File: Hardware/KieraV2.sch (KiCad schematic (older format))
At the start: 36 parts, among them J1 Conn_01x05_Male, J2 Conn_01x04_Male, SW1 SW_Rotary2x4, SW2 SW_Rotary2x4, SW3 SW_Push, SW4 SW_Push, SW5 SW_Push, SW6 SW_MEC_5G, U1 STM32L4P5RET6, Y1 8MHz

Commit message: removed resistor in crystal section
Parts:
- removed R16: 400, symbol Device:R
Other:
- moved on the sheet: C14, C15, C17, Y1
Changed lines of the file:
@@
 Text GLabel 5350 3600 0    50   Input ~ 0
 OSC_OUT
-Text GLabel 9350 2350 0    50   Input ~ 0
+Text GLabel 9450 2350 0    50   Input ~ 0
 OSC_OUT
 $Comp
 L Device:Crystal Y1
 U 1 1 61C845B0
-P 10050 2100
-F 0 "Y1" V 10004 2231 50  0000 L CNN
-F 1 "8MHz" V 10095 2231 50  0000 L CNN
-F 2 "" H 10050 2100 50  0001 C CNN
-F 3 "~" H 10050 2100 50  0001 C CNN
-	1    10050 2100
+P 9800 2100
+F 0 "Y1" V 9754 2231 50  0000 L CNN
+F 1 "8MHz" V 9845 2231 50  0000 L CNN
+F 2 "" H 9800 2100 50  0001 C CNN
+F 3 "~" H 9800 2100 50  0001 C CNN
+	1    9800 2100
 	0    1    1    0
 $EndComp
@@
 L Device:C C14
 U 1 1 61C8E389
-P 10500 1850
-F 0 "C14" V 10650 1800 50  0000 L CNN
-F 1 "10pF" V 10350 1750 50  0000 L CNN
-F 2 "" H 10538 1700 50  0001 C CNN
-F 3 "~" H 10500 1850 50  0001 C CNN
-	1    10500 1850
+P 10250 1850
+F 0 "C14" V 10400 1800 50  0000 L CNN
+F 1 "10pF" V 10100 1750 50  0000 L CNN
+F 2 "" H 10288 1700 50  0001 C CNN
+F 3 "~" H 10250 1850 50  0001 C CNN
+	1    10250 1850
 	0    -1   -1   0
 $EndComp
@@
 L Device:C C15
 U 1 1 61C92020
-P 10500 2350
-F 0 "C15" V 10650 2300 50  0000 L CNN
-F 1 "10pF" V 10350 2250 50  0000 L CNN
-F 2 "" H 10538 2200 50  0001 C CNN
-F 3 "~" H 10500 2350 50  0001 C CNN
-	1    10500 2350
+P 10250 2350
+F 0 "C15" V 10400 2300 50  0000 L CNN
+F 1 "10pF" V 10100 2250 50  0000 L CNN
+F 2 "" H 10288 2200 50  0001 C CNN
+F 3 "~" H 10250 2350 50  0001 C CNN
+	1    10250 2350
 	0    -1   -1   0
 $EndComp
@@
 L power:GND #PWR?
 U 1 1 61CA102A
-P 10850 2350
-F 0 "#PWR?" H 10850 2100 50  0001 C CNN
-F 1 "GND" H 10855 2177 50  0000 C CNN
-F 2 "" H 10850 2350 50  0001 C CNN
-F 3 "" H 10850 2350 50  0001 C CNN
-	1    10850 2350
-	1    0    0    -1
-$EndComp
-Wire Wire Line
-	10650 2350 10850 2350
-Wire Wire Line
-	10650 1850 10850 1850
-Wire Wire Line
-	10850 1850 10850 2350
-Connection ~ 10850 2350
-Wire Wire Line
-	10350 1850 10050 1850
-Wire Wire Line
-	10050 1950 10050 1850
-Wire Wire Line
-	10050 2250 10050 2350
-Text GLabel 9350 1850 0    50   Input ~ 0
+P 10600 2350
+F 0 "#PWR?" H 10600 2100 50  0001 C CNN
+F 1 "GND" H 10605 2177 50  0000 C CNN
+F 2 "" H 10600 2350 50  0001 C CNN
+F 3 "" H 10600 2350 50  0001 C CNN
+	1    10600 2350
+	1    0    0    -1
+$EndComp
+Wire Wire Line
+	10400 2350 10600 2350
+Wire Wire Line
+	10400 1850 10600 1850
+Wire Wire Line
+	10600 1850 10600 2350
+Connection ~ 10600 2350
+Wire Wire Line
+	10100 1850 9800 1850
+Wire Wire Line
+	9800 1950 9800 1850
+Wire Wire Line
+	9800 2250 9800 2350
+Text GLabel 9450 1850 0    50   Input ~ 0
 OSC_IN
-Connection ~ 10050 1850
-Wire Wire Line
-	10050 2350 10350 2350
-Wire Wire Line
-	9350 1850 10050 1850
-$Comp
-L Device:R R16
-U 1 1 61CD4DE5
-P 9700 2350
-F 0 "R16" V 9493 2350 50  0000 C CNN
-F 1 "400" V 9584 2350 50  0000 C CNN
-F 2 "" V 9630 2350 50  0001 C CNN
-F 3 "~" H 9700 2350 50  0001 C CNN
-	1    9700 2350
-	0    1    1    0
-$EndComp
-Wire Wire Line
-	9550 2350 9350 2350
-Wire Wire Line
-	9850 2350 10050 2350
-Connection ~ 10050 2350
+Wire Wire Line
+	9800 2350 10100 2350
 Wire Notes Line
 	4800 7750 4800 5350
@@
 Text Notes 1750 650  0    79   ~ 0
 SWITCHES
-Wire Wire Line
-	4150 5800 3950 5800
 $Comp
 L power:GND #PWR?
 U 1 1 61BB611A
-P 4150 6100
-F 0 "#PWR?" H 4150 5850 50  0001 C CNN
-F 1 "GND" H 4155 5927 50  0000 C CNN
-F 2 "" H 4150 6100 50  0001 C CNN
-F 3 "" H 4150 6100 50  0001 C CNN
-	1    4150 6100
-	1    0    0    -1
-$EndComp
-Text GLabel 3950 5800 0    50   Input ~ 0
+P 4250 6100
+F 0 "#PWR?" H 4250 5850 50  0001 C CNN
+F 1 "GND" H 4255 5927 50  0000 C CNN
+F 2 "" H 4250 6100 50  0001 C CNN
+F 3 "" H 4250 6100 50  0001 C CNN
+	1    4250 6100
+	1    0    0    -1
+$EndComp
+Text GLabel 3850 5800 0    50   Input ~ 0
 VBAT
 Wire Notes Line
@@
 L Device:C C17
 U 1 1 61E85A6A
-P 4150 5950
-F 0 "C17" H 4265 5996 50  0000 L CNN
-F 1 "100nF" H 4265 5905 50  0000 L CNN
-F 2 "" H 4188 5800 50  0001 C CNN
-F 3 "~" H 4150 5950 50  0001 C CNN
-	1    4150 5950
+P 4250 5950
+F 0 "C17" H 4365 5996 50  0000 L CNN
+F 1 "100nF" H 4365 5905 50  0000 L CNN
+F 2 "" H 4288 5800 50  0001 C CNN
+F 3 "~" H 4250 5950 50  0001 C CNN
+	1    4250 5950
 	1    0    0    -1
 $EndComp
@@
 L power:+3.3V #PWR?
 U 1 1 61EA71EF
-P 4150 5800
-F 0 "#PWR?" H 4150 5650 50  0001 C CNN
-F 1 "+3.3V" H 4165 5973 50  0000 C CNN
-F 2 "" H 4150 5800 50  0001 C CNN
-F 3 "" H 4150 5800 50  0001 C CNN
-	1    4150 5800
+P 4050 5800
+F 0 "#PWR?" H 4050 5650 50  0001 C CNN
+F 1 "+3.3V" H 4065 5973 50  0000 C CNN
+F 2 "" H 4050 5800 50  0001 C CNN
+F 3 "" H 4050 5800 50  0001 C CNN
+	1    4050 5800
 	1    0    0    -1
 $EndComp
@@
 Wire Wire Line
 	8400 850  8400 800
+Wire Wire Line
+	9450 1850 9800 1850
+Connection ~ 9800 1850
+Wire Wire Line
+	9800 2350 9450 2350
+Connection ~ 9800 2350
+Wire Wire Line
+	4250 5800 4050 5800
+Wire Wire Line
+	3850 5800 4050 5800
+Connection ~ 4050 5800
 $EndSCHEMATC

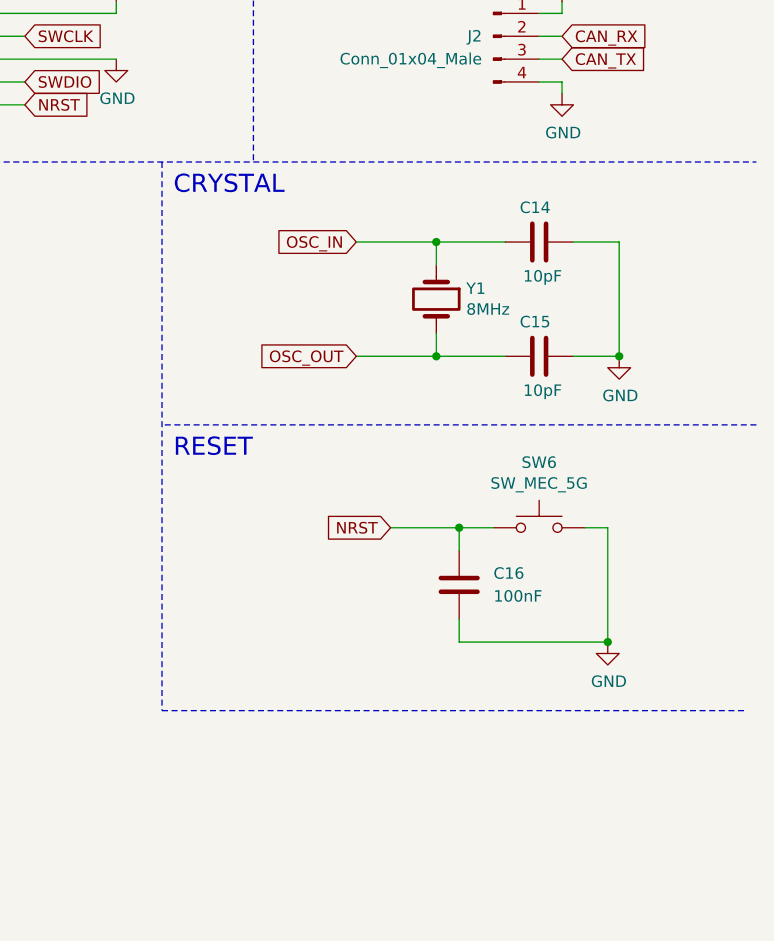
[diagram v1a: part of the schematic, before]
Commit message: 10k resistor in reset
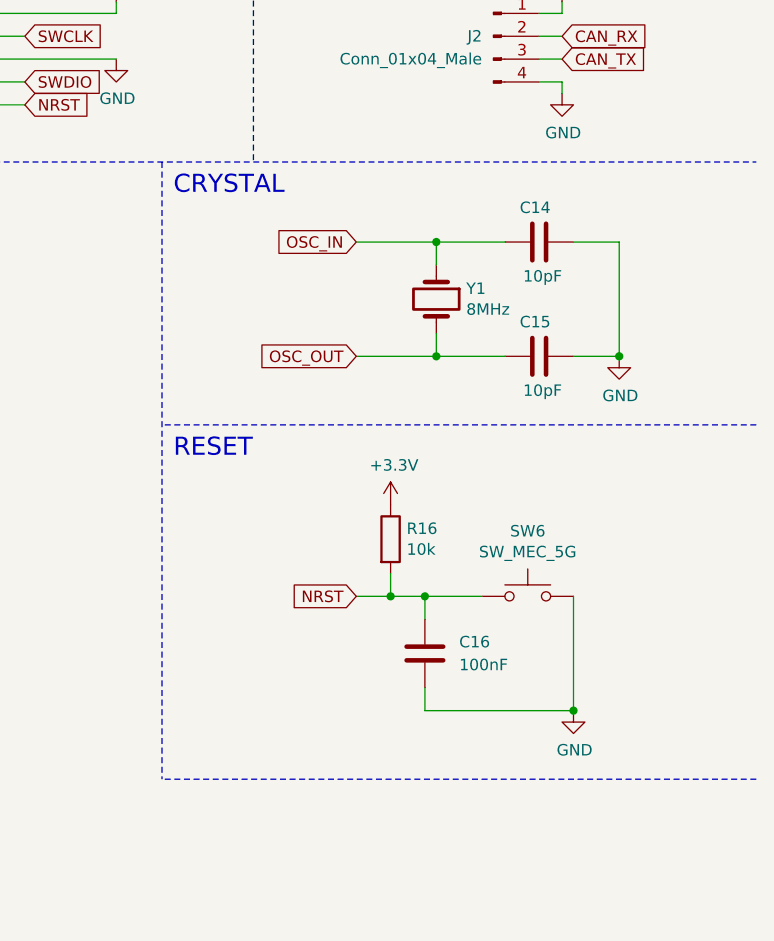
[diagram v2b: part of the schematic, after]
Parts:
- added R16: 10k, symbol Device:R
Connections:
- wire segments 141 -> 142
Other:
- moved on the sheet: C16, SW6
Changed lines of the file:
@@
 Text Notes 8650 1650 0    79   ~ 0
 CRYSTAL
-Text GLabel 9600 3100 0    50   Input ~ 0
+Text GLabel 9450 3400 0    50   Input ~ 0
 NRST
-$Comp
-L Device:C C16
-U 1 1 61DAE754
-P 9900 3350
-F 0 "C16" H 10050 3400 50  0000 L CNN
-F 1 "100nF" H 10050 3300 50  0000 L CNN
-F 2 "" H 9938 3200 50  0001 C CNN
-F 3 "~" H 9900 3350 50  0001 C CNN
-	1    9900 3350
-	1    0    0    -1
-$EndComp
-$Comp
-L Switch:SW_MEC_5G SW6
-U 1 1 61DC36EF
-P 10250 3100
-F 0 "SW6" H 10250 3385 50  0000 C CNN
-F 1 "SW_MEC_5G" H 10250 3294 50  0000 C CNN
-F 2 "" H 10250 3300 50  0001 C CNN
-F 3 "http://www.apem.com/int/index.php?controller=attachment&id_attachment=488" H 10250 3300 50  0001 C CNN
-	1    10250 3100
-	1    0    0    -1
-$EndComp
 $Comp
 L power:GND #PWR?
 U 1 1 61DCF62E
-P 10550 3600
-F 0 "#PWR?" H 10550 3350 50  0001 C CNN
-F 1 "GND" H 10555 3427 50  0000 C CNN
-F 2 "" H 10550 3600 50  0001 C CNN
-F 3 "" H 10550 3600 50  0001 C CNN
-	1    10550 3600
+P 10400 3900
+F 0 "#PWR?" H 10400 3650 50  0001 C CNN
+F 1 "GND" H 10405 3727 50  0000 C CNN
+F 2 "" H 10400 3900 50  0001 C CNN
+F 3 "" H 10400 3900 50  0001 C CNN
+	1    10400 3900
 	1    0    0    -1
 $EndComp
 Wire Wire Line
-	10550 3600 9900 3600
+	10400 3900 9750 3900
 Wire Wire Line
-	9900 3600 9900 3500
+	9750 3900 9750 3800
 Wire Wire Line
-	10550 3600 10550 3100
-Connection ~ 10550 3600
-Wire Wire Line
-	9900 3200 9900 3100
-Wire Wire Line
-	9600 3100 9900 3100
-Wire Wire Line
-	10550 3100 10450 3100
-Wire Wire Line
-	10050 3100 9900 3100
-Connection ~ 9900 3100
-Wire Notes Line
-	8600 3900 11150 3900
-Wire Notes Line
-	8600 1500 8600 3900
+	9450 3400 9600 3400
 Text Notes 8650 2800 0    79   ~ 0
 RESET
@@
 	3850 5800 4050 5800
 Connection ~ 4050 5800
+$Comp
+L Device:R R16
+U 1 1 61A43041
+P 9600 3150
+F 0 "R16" H 9670 3196 50  0000 L CNN
+F 1 "10k" H 9670 3105 50  0000 L CNN
+F 2 "" V 9530 3150 50  0001 C CNN
+F 3 "~" H 9600 3150 50  0001 C CNN
+	1    9600 3150
+	1    0    0    -1
+$EndComp
+$Comp
+L Switch:SW_MEC_5G SW6
+U 1 1 61DC36EF
+P 10200 3400
+F 0 "SW6" H 10200 3685 50  0000 C CNN
+F 1 "SW_MEC_5G" H 10200 3594 50  0000 C CNN
+F 2 "" H 10200 3600 50  0001 C CNN
+F 3 "http://www.apem.com/int/index.php?controller=attachment&id_attachment=488" H 10200 3600 50  0001 C CNN
+	1    10200 3400
+	1    0    0    -1
+$EndComp
+Wire Wire Line
+	10400 3400 10400 3900
+Connection ~ 10400 3900
+Wire Wire Line
+	9600 3400 9600 3300
+$Comp
+L power:+3.3V #PWR?
+U 1 1 61A6B2EC
+P 9600 3000
+F 0 "#PWR?" H 9600 2850 50  0001 C CNN
+F 1 "+3.3V" H 9615 3173 50  0000 C CNN
+F 2 "" H 9600 3000 50  0001 C CNN
+F 3 "" H 9600 3000 50  0001 C CNN
+	1    9600 3000
+	1    0    0    -1
+$EndComp
+Connection ~ 9600 3400
+Wire Wire Line
+	9600 3400 9750 3400
+Wire Wire Line
+	9750 3400 10000 3400
+Connection ~ 9750 3400
+Wire Wire Line
+	9750 3500 9750 3400
+$Comp
+L Device:C C16
+U 1 1 61DAE754
+P 9750 3650
+F 0 "C16" H 9900 3700 50  0000 L CNN
+F 1 "100nF" H 9900 3600 50  0000 L CNN
+F 2 "" H 9788 3500 50  0001 C CNN
+F 3 "~" H 9750 3650 50  0001 C CNN
+	1    9750 3650
+	1    0    0    -1
+$EndComp
+Wire Notes Line
+	11200 4200 8600 4200
+Wire Notes Line
+	8600 1500 8600 4200
 $EndSCHEMATC

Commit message: RC added by pushbuttons, changed capacitors in uC supply
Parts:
- removed C13: 1uF, symbol Device:CP
- removed C9: 4.7uF, symbol Device:CP
- added C13, C9: 1uF, symbol Device:C
- added C18, C19, C20: 100nF, symbol Device:C
- added R17, R18, R19: 1k, symbol Device:R
- C11: value 10nF -> 100nF
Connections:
- wire segments 142 -> 149
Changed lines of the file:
@@
 $EndComp
 $Comp
-L power:GND #PWR?
+L power:GND #PWR09
 U 1 1 61A51CFB
 P 3250 1750
-F 0 "#PWR?" H 3250 1500 50  0001 C CNN
+F 0 "#PWR09" H 3250 1500 50  0001 C CNN
 F 1 "GND" H 3255 1577 50  0000 C CNN
 F 2 "" H 3250 1750 50  0001 C CNN
@@
 $EndComp
 $Comp
-L power:GND #PWR?
+L power:GND #PWR010
 U 1 1 61A52714
 P 3250 2700
-F 0 "#PWR?" H 3250 2450 50  0001 C CNN
+F 0 "#PWR010" H 3250 2450 50  0001 C CNN
 F 1 "GND" H 3255 2527 50  0000 C CNN
 F 2 "" H 3250 2700 50  0001 C CNN
@@
 $EndComp
 $Comp
-L power:+3.3V #PWR?
+L power:+3.3V #PWR01
 U 1 1 61A6C179
 P 750 800
-F 0 "#PWR?" H 750 650 50  0001 C CNN
+F 0 "#PWR01" H 750 650 50  0001 C CNN
 F 1 "+3.3V" H 765 973 50  0000 C CNN
 F 2 "" H 750 800 50  0001 C CNN
@@
 $EndComp
 $Comp
-L power:GND #PWR?
+L power:GND #PWR04
 U 1 1 61A86101
 P 2100 3500
-F 0 "#PWR?" H 2100 3250 50  0001 C CNN
+F 0 "#PWR04" H 2100 3250 50  0001 C CNN
 F 1 "GND" H 2105 3327 50  0000 C CNN
 F 2 "" H 2100 3500 50  0001 C CNN
@@
 $EndComp
 $Comp
-L power:GND #PWR?
+L power:GND #PWR05
 U 1 1 61A8713E
 P 2100 4100
-F 0 "#PWR?" H 2100 3850 50  0001 C CNN
+F 0 "#PWR05" H 2100 3850 50  0001 C CNN
 F 1 "GND" H 2105 3927 50  0000 C CNN
 F 2 "" H 2100 4100 50  0001 C CNN
@@
 $EndComp
 $Comp
-L power:GND #PWR?
+L power:GND #PWR06
 U 1 1 61A880AF
 P 2100 4700
-F 0 "#PWR?" H 2100 4450 50  0001 C CNN
+F 0 "#PWR06" H 2100 4450 50  0001 C CNN
 F 1 "GND" H 2105 4527 50  0000 C CNN
 F 2 "" H 2100 4700 50  0001 C CNN
@@
 Connection ~ 2100 4400
 Wire Wire Line
-	2100 4400 2900 4400
-Wire Wire Line
-	1650 3800 2100 3800
-Wire Wire Line
-	2100 3800 2900 3800
+	2100 4400 2450 4400
+Wire Wire Line
+	1650 3800 1700 3800
+Wire Wire Line
+	2100 3800 2450 3800
 Wire Wire Line
 	1650 3200 2100 3200
 Connection ~ 2100 3200
 Wire Wire Line
-	2100 3200 2900 3200
+	2100 3200 2450 3200
 Connection ~ 750  3800
 Wire Wire Line
@@
 NRST
 $Comp
-L power:GND #PWR?
+L power:GND #PWR025
 U 1 1 61A4CEAD
 P 8400 1050
-F 0 "#PWR?" H 8400 800 50  0001 C CNN
+F 0 "#PWR025" H 8400 800 50  0001 C CNN
 F 1 "GND" H 8405 877 50  0000 C CNN
 F 2 "" H 8400 1050 50  0001 C CNN
@@
 	7850 1250 8000 1250
 $Comp
-L power:GND #PWR?
+L power:GND #PWR015
 U 1 1 61A87240
 P 6200 6250
-F 0 "#PWR?" H 6200 6000 50  0001 C CNN
+F 0 "#PWR015" H 6200 6000 50  0001 C CNN
 F 1 "GND" H 6205 6077 50  0000 C CNN
 F 2 "" H 6200 6250 50  0001 C CNN
@@
 CAN_RX
 $Comp
-L power:+5V #PWR?
+L power:+5V #PWR027
 U 1 1 61A9DC54
 P 10350 800
-F 0 "#PWR?" H 10350 650 50  0001 C CNN
+F 0 "#PWR027" H 10350 650 50  0001 C CNN
 F 1 "+5V" H 10365 973 50  0000 C CNN
 F 2 "" H 10350 800 50  0001 C CNN
@@
 $EndComp
 $Comp
-L power:GND #PWR?
+L power:GND #PWR028
 U 1 1 61A9F0B3
 P 10350 1200
-F 0 "#PWR?" H 10350 950 50  0001 C CNN
+F 0 "#PWR028" H 10350 950 50  0001 C CNN
 F 1 "GND" H 10355 1027 50  0000 C CNN
 F 2 "" H 10350 1200 50  0001 C CNN
@@
 P 1700 7200
 F 0 "C11" H 1815 7246 50  0000 L CNN
-F 1 "10nF" H 1815 7155 50  0000 L CNN
+F 1 "100nF" H 1815 7155 50  0000 L CNN
 F 2 "" H 1738 7050 50  0001 C CNN
 F 3 "~" H 1700 7200 50  0001 C CNN
@@
 $EndComp
 $Comp
-L Device:CP C13
-U 1 1 61B47BB4
-P 2700 7200
-F 0 "C13" H 2818 7246 50  0000 L CNN
-F 1 "1uF" H 2818 7155 50  0000 L CNN
-F 2 "" H 2738 7050 50  0001 C CNN
-F 3 "~" H 2700 7200 50  0001 C CNN
-	1    2700 7200
-	1    0    0    -1
-$EndComp
-$Comp
-L power:+3.3V #PWR?
+L power:+3.3V #PWR03
 U 1 1 61B52FBA
 P 1450 6950
-F 0 "#PWR?" H 1450 6800 50  0001 C CNN
+F 0 "#PWR03" H 1450 6800 50  0001 C CNN
 F 1 "+3.3V" H 1465 7123 50  0000 C CNN
 F 2 "" H 1450 6950 50  0001 C CNN
 F 3 "" H 1450 6950 50  0001 C CNN
 	1    1450 6950
-	1    0    0    -1
-$EndComp
-$Comp
-L Device:CP C9
-U 1 1 61B579CD
-P 2800 5950
-F 0 "C9" H 2918 5996 50  0000 L CNN
-F 1 "4.7uF" H 2918 5905 50  0000 L CNN
-F 2 "" H 2838 5800 50  0001 C CNN
-F 3 "~" H 2800 5950 50  0001 C CNN
-	1    2800 5950
 	1    0    0    -1
 $EndComp
@@
 Wire Wire Line
 	2300 5700 2800 5700
-Wire Wire Line
-	2800 5700 2800 5800
 Connection ~ 2300 5700
 Wire Wire Line
@@
 Connection ~ 1300 5700
 $Comp
-L power:+3.3V #PWR?
+L power:+3.3V #PWR02
 U 1 1 61B8345C
 P 1050 5650
-F 0 "#PWR?" H 1050 5500 50  0001 C CNN
+F 0 "#PWR02" H 1050 5500 50  0001 C CNN
 F 1 "+3.3V" H 1065 5823 50  0000 C CNN
 F 2 "" H 1050 5650 50  0001 C CNN
@@
 	1050 5700 1300 5700
 $Comp
-L power:GND #PWR?
+L power:GND #PWR08
 U 1 1 61B9E8D8
 P 2800 6250
-F 0 "#PWR?" H 2800 6000 50  0001 C CNN
+F 0 "#PWR08" H 2800 6000 50  0001 C CNN
 F 1 "GND" H 2805 6077 50  0000 C CNN
 F 2 "" H 2800 6250 50  0001 C CNN
@@
 Connection ~ 2800 6200
 $Comp
-L power:GND #PWR?
+L power:GND #PWR07
 U 1 1 61BA45BC
 P 2700 7450
-F 0 "#PWR?" H 2700 7200 50  0001 C CNN
+F 0 "#PWR07" H 2700 7200 50  0001 C CNN
 F 1 "GND" H 2705 7277 50  0000 C CNN
 F 2 "" H 2700 7450 50  0001 C CNN
@@
 Text GLabel 3850 7050 0    50   Input ~ 0
 VDDUSB
-Text GLabel 1200 6950 0    50   Input ~ 0
-VREF+
 $Comp
 L Device:C C10
@@
 	3850 7050 4050 7050
 $Comp
-L power:GND #PWR?
+L power:GND #PWR014
 U 1 1 61BD088B
 P 4250 7350
-F 0 "#PWR?" H 4250 7100 50  0001 C CNN
+F 0 "#PWR014" H 4250 7100 50  0001 C CNN
 F 1 "GND" H 4255 7177 50  0000 C CNN
 F 2 "" H 4250 7350 50  0001 C CNN
@@
 $EndComp
 $Comp
-L power:+3.3V #PWR?
+L power:+3.3V #PWR012
 U 1 1 61BD3BB2
 P 4050 7050
-F 0 "#PWR?" H 4050 6900 50  0001 C CNN
+F 0 "#PWR012" H 4050 6900 50  0001 C CNN
 F 1 "+3.3V" H 4065 7223 50  0000 C CNN
 F 2 "" H 4050 7050 50  0001 C CNN
@@
 Wire Wire Line
 	1200 6950 1450 6950
-Wire Wire Line
-	2700 6950 2700 7050
 Connection ~ 1450 6950
 Wire Wire Line
@@
 $EndComp
 $Comp
-L power:GND #PWR?
+L power:GND #PWR030
 U 1 1 61CA102A
 P 10600 2350
-F 0 "#PWR?" H 10600 2100 50  0001 C CNN
+F 0 "#PWR030" H 10600 2100 50  0001 C CNN
 F 1 "GND" H 10605 2177 50  0000 C CNN
 F 2 "" H 10600 2350 50  0001 C CNN
@@
 NRST
 $Comp
-L power:GND #PWR?
+L power:GND #PWR029
 U 1 1 61DCF62E
 P 10400 3900
-F 0 "#PWR?" H 10400 3650 50  0001 C CNN
+F 0 "#PWR029" H 10400 3650 50  0001 C CNN
 F 1 "GND" H 10405 3727 50  0000 C CNN
 F 2 "" H 10400 3900 50  0001 C CNN
@@
 SWITCHES
 $Comp
-L power:GND #PWR?
+L power:GND #PWR013
 U 1 1 61BB611A
 P 4250 6100
-F 0 "#PWR?" H 4250 5850 50  0001 C CNN
+F 0 "#PWR013" H 4250 5850 50  0001 C CNN
 F 1 "GND" H 4255 5927 50  0000 C CNN
 F 2 "" H 4250 6100 50  0001 C CNN
@@
 Text GLabel 3850 5800 0    50   Input ~ 0
 VBAT
-Wire Notes Line
-	3250 5350 3250 7750
 $Comp
 L Device:C C17
@@
 $EndComp
 $Comp
-L power:+3.3V #PWR?
+L power:+3.3V #PWR011
 U 1 1 61EA71EF
 P 4050 5800
-F 0 "#PWR?" H 4050 5650 50  0001 C CNN
+F 0 "#PWR011" H 4050 5650 50  0001 C CNN
 F 1 "+3.3V" H 4065 5973 50  0000 C CNN
 F 2 "" H 4050 5800 50  0001 C CNN
@@
 +3V3
 $Comp
-L power:+3.3V #PWR?
+L power:+3.3V #PWR024
 U 1 1 61B51C6E
 P 8400 800
-F 0 "#PWR?" H 8400 650 50  0001 C CNN
+F 0 "#PWR024" H 8400 650 50  0001 C CNN
 F 1 "+3.3V" H 8415 973 50  0000 C CNN
 F 2 "" H 8400 800 50  0001 C CNN
@@
 	9600 3400 9600 3300
 $Comp
-L power:+3.3V #PWR?
+L power:+3.3V #PWR026
 U 1 1 61A6B2EC
 P 9600 3000
-F 0 "#PWR?" H 9600 2850 50  0001 C CNN
+F 0 "#PWR026" H 9600 2850 50  0001 C CNN
 F 1 "+3.3V" H 9615 3173 50  0000 C CNN
 F 2 "" H 9600 3000 50  0001 C CNN
@@
 Wire Notes Line
 	8600 1500 8600 4200
+Wire Wire Line
+	2700 7050 2700 6950
+Text GLabel 1200 6950 0    50   Input ~ 0
+VREF+
+$Comp
+L Device:C C13
+U 1 1 61A748B1
+P 2700 7200
+F 0 "C13" H 2815 7246 50  0000 L CNN
+F 1 "1uF" H 2815 7155 50  0000 L CNN
+F 2 "" H 2738 7050 50  0001 C CNN
+F 3 "~" H 2700 7200 50  0001 C CNN
+	1    2700 7200
+	1    0    0    -1
+$EndComp
+Wire Notes Line
+	3250 5350 3250 7750
+Wire Wire Line
+	2800 5800 2800 5700
+$Comp
+L Device:C C9
+U 1 1 61A8C773
+P 2800 5950
+F 0 "C9" H 2915 5996 50  0000 L CNN
+F 1 "1uF" H 2915 5905 50  0000 L CNN
+F 2 "" H 2838 5800 50  0001 C CNN
+F 3 "~" H 2800 5950 50  0001 C CNN
+	1    2800 5950
+	1    0    0    -1
+$EndComp
+$Comp
+L Device:C C19
+U 1 1 61A95079
+P 2450 3950
+F 0 "C19" H 2565 3996 50  0000 L CNN
+F 1 "100nF" H 2565 3905 50  0000 L CNN
+F 2 "" H 2488 3800 50  0001 C CNN
+F 3 "~" H 2450 3950 50  0001 C CNN
+	1    2450 3950
+	1    0    0    -1
+$EndComp
+Wire Wire Line
+	2450 4100 2100 4100
+Connection ~ 2100 4100
+Connection ~ 2450 3800
+Wire Wire Line
+	2450 3800 2900 3800
+$Comp
+L Device:R R18
+U 1 1 61AB2BD3
+P 1850 3800
+F 0 "R18" H 1700 3750 50  0000 C CNN
+F 1 "1k" H 1700 3850 50  0000 C CNN
+F 2 "" V 1780 3800 50  0001 C CNN
+F 3 "~" H 1850 3800 50  0001 C CNN
+	1    1850 3800
+	0    1    1    0
+$EndComp
+Wire Wire Line
+	2000 3800 2100 3800
+$Comp
+L Device:R R17
+U 1 1 61AD0520
+P 1850 3200
+F 0 "R17" H 1700 3150 50  0000 C CNN
+F 1 "1k" H 1700 3250 50  0000 C CNN
+F 2 "" V 1780 3200 50  0001 C CNN
+F 3 "~" H 1850 3200 50  0001 C CNN
+	1    1850 3200
+	0    1    1    0
+$EndComp
+$Comp
+L Device:R R19
+U 1 1 61AD6247
+P 1850 4400
+F 0 "R19" H 1700 4350 50  0000 C CNN
+F 1 "1k" H 1700 4450 50  0000 C CNN
+F 2 "" V 1780 4400 50  0001 C CNN
+F 3 "~" H 1850 4400 50  0001 C CNN
+	1    1850 4400
+	0    1    1    0
+$EndComp
+$Comp
+L Device:C C20
+U 1 1 61ADBF30
+P 2450 4550
+F 0 "C20" H 2565 4596 50  0000 L CNN
+F 1 "100nF" H 2565 4505 50  0000 L CNN
+F 2 "" H 2488 4400 50  0001 C CNN
+F 3 "~" H 2450 4550 50  0001 C CNN
+	1    2450 4550
+	1    0    0    -1
+$EndComp
+Wire Wire Line
+	2450 4700 2100 4700
+$Comp
+L Device:C C18
+U 1 1 61AE1E72
+P 2450 3350
+F 0 "C18" H 2565 3396 50  0000 L CNN
+F 1 "100nF" H 2565 3305 50  0000 L CNN
+F 2 "" H 2488 3200 50  0001 C CNN
+F 3 "~" H 2450 3350 50  0001 C CNN
+	1    2450 3350
+	1    0    0    -1
+$EndComp
+Wire Wire Line
+	2450 3500 2100 3500
+Connection ~ 2450 3200
+Wire Wire Line
+	2450 3200 2900 3200
+Connection ~ 2450 4400
+Wire Wire Line
+	2450 4400 2900 4400
 $EndSCHEMATC

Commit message: changed global labels to local, added IMU
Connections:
- net labels added: CAN+, CAN-, IMU_INT1, IMU_INT2, IMU_SPI1_CLK, IMU_SPI1_CS, IMU_SPI1_MISO, IMU_SPI1_MOSI, IMU_SPI1_NSS, IMU_SPI1_SCK
- net labels removed: CAN1_RX, CAN1_TX
- wire segments 149 -> 169
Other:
- note added: "+3V3"
- note added: "+5V\n"
- note added: "IMU\n"
- moved on the sheet: J1
